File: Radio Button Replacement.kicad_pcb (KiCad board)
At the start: 2 copper layers, 40 x 40 mm, 19 parts, among them SW1 SW_Push_SPDT_1_3_2, SW2 SW_Push_SPDT_1_3_2, SW3 SW_Push_SPDT_1_3_2, SW4 SW_Push_SPDT_1_3_2

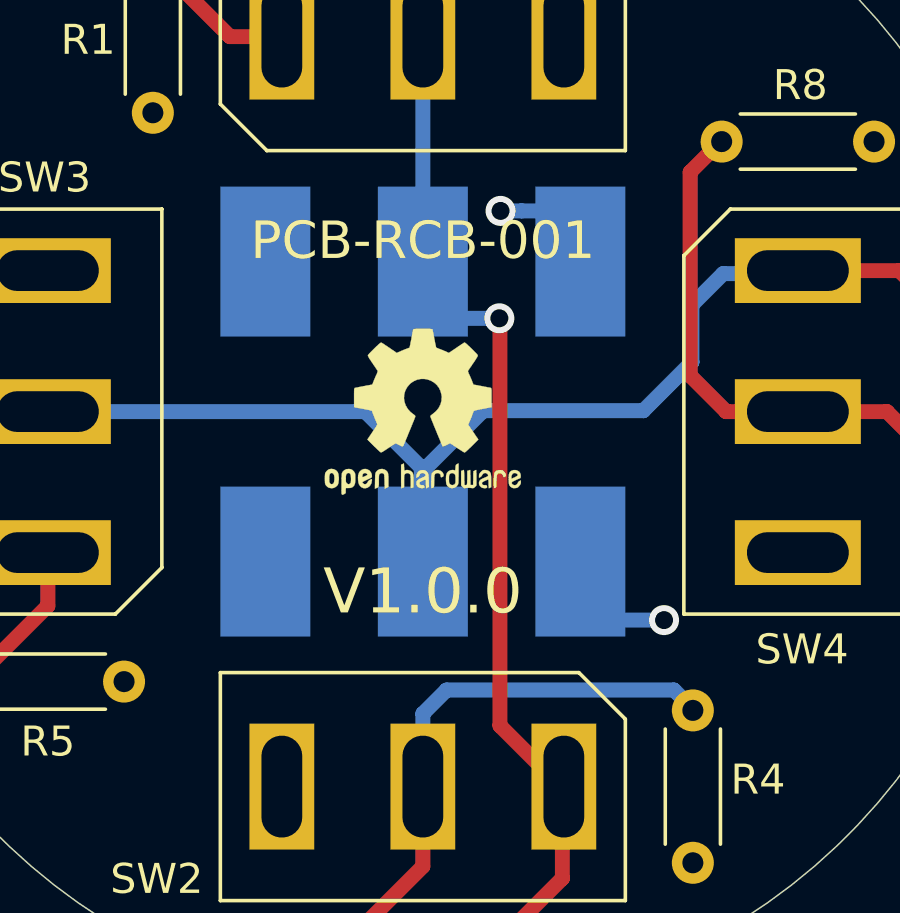
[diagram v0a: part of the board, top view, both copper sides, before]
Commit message: Update Radio Button Replacement.kicad_pcb
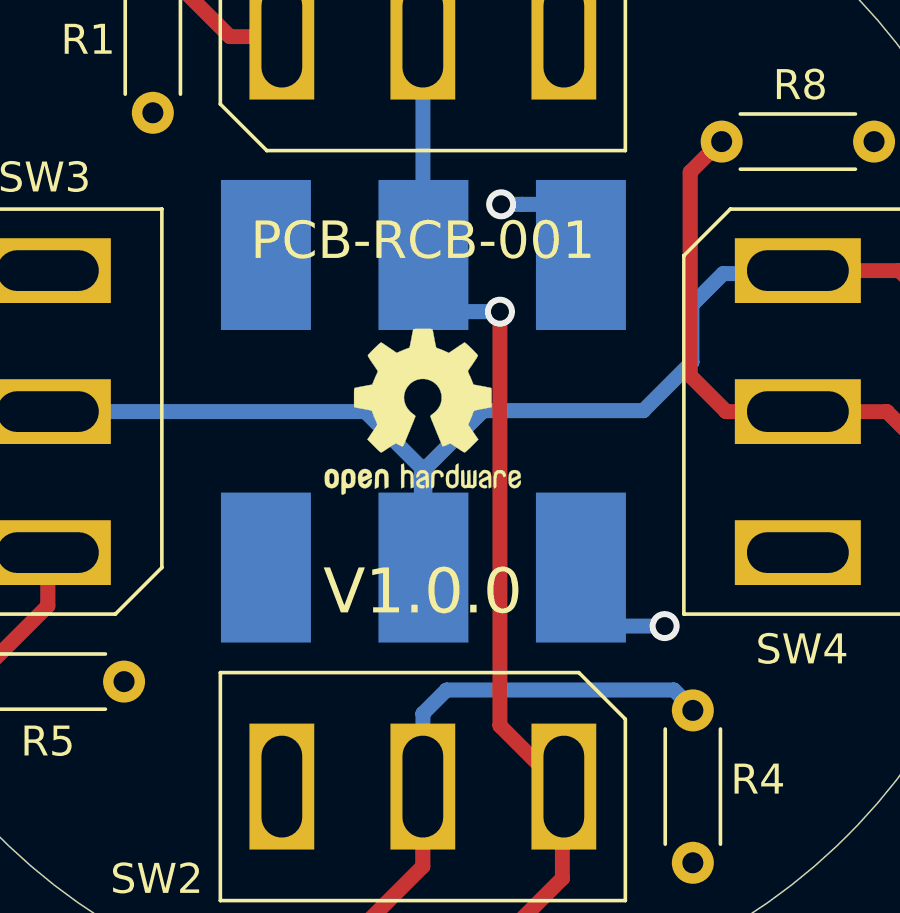
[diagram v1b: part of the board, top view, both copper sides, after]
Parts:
- moved TP1 0.22 mm to (150.0, 94.8)
- moved TP2 0.20 mm to (150.0, 105.2)
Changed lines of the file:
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@@
     (thickness 1.6)
     (drawings 5)
-    (tracks 68)
+    (tracks 67)
     (zones 0)
     (modules 19)
@@
     (31 B.Cu signal)
     (32 B.Adhes user)
-    (33 F.Adhes user hide)
+    (33 F.Adhes user)
     (34 B.Paste user)
     (35 F.Paste user)
     (36 B.SilkS user)
-    (37 F.SilkS user)
+    (37 F.SilkS user hide)
     (38 B.Mask user)
     (39 F.Mask user)
@@
   )
   (module Frequently_Used_LE:Pad_3_3.0-5.0 (layer B.Cu)
-    (at 150 105)
+    (at 150.02 105.2)
     (descr "SMD Pad 3.0x5.0 mm")
     (attr smd)
@@
       (effects (font (size 1 1) (thickness 0.15)) (justify top mirror))
     )
-    (fp_text user - (at -5.25 4.25) (layer B.SilkS)
+    (fp_text user - (at -5.22 -3.97) (layer B.SilkS)
       (effects (font (size 1.5 1.5) (thickness 0.3)) (justify mirror))
     )
-    (fp_text user S (at 0 4.25) (layer B.SilkS)
+    (fp_text user S (at 0.03 -3.97) (layer B.SilkS)
       (effects (font (size 1.5 1.5) (thickness 0.3)) (justify mirror))
     )
@@
     (fp_line (start 7.5 -3.25) (end -7.5 -3.25) (layer B.CrtYd) (width 0.05))
     (fp_line (start 7.5 3.25) (end 7.5 -3.25) (layer B.CrtYd) (width 0.05))
-    (fp_text user + (at 5.25 4.25) (layer B.SilkS)
+    (fp_text user + (at 5.28 -3.97) (layer B.SilkS)
       (effects (font (size 1.5 1.5) (thickness 0.3)) (justify mirror))
     )
@@
   )
   (module Frequently_Used_LE:Pad_3_3.0-5.0 (layer B.Cu)
-    (at 150 95)
+    (at 150.02 94.78)
     (descr "SMD Pad 3.0x5.0 mm")
     (attr smd)
@@
       (effects (font (size 1 1) (thickness 0.15)) (justify top mirror))
     )
-    (fp_text user - (at -5.25 4.25) (layer B.SilkS)
+    (fp_text user - (at -5.21 4.1) (layer B.SilkS)
       (effects (font (size 1.5 1.5) (thickness 0.3)) (justify mirror))
     )
-    (fp_text user S (at 0 4.25) (layer B.SilkS)
+    (fp_text user S (at 0.04 4.1) (layer B.SilkS)
       (effects (font (size 1.5 1.5) (thickness 0.3)) (justify mirror))
     )
@@
     (fp_line (start 7.5 -3.25) (end -7.5 -3.25) (layer B.CrtYd) (width 0.05))
     (fp_line (start 7.5 3.25) (end 7.5 -3.25) (layer B.CrtYd) (width 0.05))
-    (fp_text user + (at 5.25 4.25) (layer B.SilkS)
+    (fp_text user + (at 5.29 4.1) (layer B.SilkS)
       (effects (font (size 1.5 1.5) (thickness 0.3)) (justify mirror))
     )
@@
     (effects (font (size 1.25 1.25) (thickness 0.25)))
   )
-  (gr_text 2 (at 158.5 104.88) (layer B.SilkS)
+  (gr_text 2 (at 158.52 105.08) (layer B.SilkS)
     (effects (font (size 1.5 1.5) (thickness 0.3)) (justify mirror))
   )
-  (gr_text 1 (at 158.5 94.88) (layer B.SilkS)
+  (gr_text 1 (at 158.52 94.66) (layer B.SilkS)
     (effects (font (size 1.5 1.5) (thickness 0.3)) (justify mirror))
   )
@@
   (segment (start 150 95) (end 150 87.51) (width 0.5) (layer B.Cu) (net 3))
   (segment (start 145.44 112.6) (end 145.46 112.58) (width 0.5) (layer B.Cu) (net 0))
-  (via (at 158.04 106.95) (size 1) (drill 0.6) (layers F.Cu B.Cu) (net 1))
-  (segment (start 156.27 106.95) (end 158.04 106.95) (width 0.5) (layer B.Cu) (net 1))
+  (via (at 158.06 107.15) (size 1) (drill 0.6) (layers F.Cu B.Cu) (net 1))
+  (segment (start 156.29 107.15) (end 158.06 107.15) (width 0.5) (layer B.Cu) (net 1))
   (segment (start 155.25 105) (end 155.25 105.93) (width 0.5) (layer B.Cu) (net 1))
   (segment (start 155.25 105.93) (end 156.27 106.95) (width 0.5) (layer B.Cu) (net 1))
-  (via (at 152.59 93.31) (size 1) (drill 0.6) (layers F.Cu B.Cu) (net 1))
-  (segment (start 153.297106 93.31) (end 152.59 93.31) (width 0.5) (layer B.Cu) (net 1))
-  (segment (start 154.31 93.31) (end 153.297106 93.31) (width 0.5) (layer B.Cu) (net 1))
+  (via (at 152.61 93.09) (size 1) (drill 0.6) (layers F.Cu B.Cu) (net 1))
+  (segment (start 153.317106 93.09) (end 152.61 93.09) (width 0.5) (layer B.Cu) (net 1))
+  (segment (start 154.33 93.09) (end 153.317106 93.09) (width 0.5) (layer B.Cu) (net 1))
   (segment (start 155.25 95) (end 155.25 94.25) (width 0.5) (layer B.Cu) (net 1))
   (segment (start 155.25 94.25) (end 154.31 93.31) (width 0.5) (layer B.Cu) (net 1))
@@
   (segment (start 145.3 84.43) (end 147.41 82.32) (width 0.5) (layer F.Cu) (net 2))
   (segment (start 150.04 87.4) (end 150.19 87.55) (width 0.5) (layer B.Cu) (net 3))
-  (via (at 152.55 96.89) (size 1) (drill 0.6) (layers F.Cu B.Cu) (net 3))
-  (segment (start 150.55 96.89) (end 152.55 96.89) (width 0.5) (layer B.Cu) (net 3))
+  (via (at 152.57 96.67) (size 1) (drill 0.6) (layers F.Cu B.Cu) (net 3))
+  (segment (start 150.57 96.67) (end 152.57 96.67) (width 0.5) (layer B.Cu) (net 3))
   (segment (start 150 95) (end 150 96.34) (width 0.5) (layer B.Cu) (net 3))
   (segment (start 150 96.34) (end 150.55 96.89) (width 0.5) (layer B.Cu) (net 3))
-  (segment (start 152.57 96.91) (end 152.55 96.89) (width 0.5) (layer F.Cu) (net 3))
-  (segment (start 154.75 112.65) (end 152.57 110.47) (width 0.5) (layer F.Cu) (net 3))
-  (segment (start 152.57 110.47) (end 152.57 96.91) (width 0.5) (layer F.Cu) (net 3))
   (segment (start 154.65 115.56) (end 154.65 112.48) (width 0.5) (layer F.Cu) (net 3))
   (segment (start 152.55 117.66) (end 154.65 115.56) (width 0.5) (layer F.Cu) (net 3))
   (segment (start 150 87.5) (end 150 84.83) (width 0.5) (layer F.Cu) (net 3))
   (segment (start 150 84.83) (end 152.54 82.29) (width 0.5) (layer F.Cu) (net 3))
+  (segment (start 152.57 110.47) (end 152.57 96.67) (width 0.5) (layer F.Cu) (net 3))
+  (segment (start 154.75 112.65) (end 152.57 110.47) (width 0.5) (layer F.Cu) (net 3))
   (segment (start 158.98 109.84) (end 159 109.86) (width 0.5) (layer B.Cu) (net 4))
   (segment (start 150 110.07) (end 150.79 109.28) (width 0.5) (layer B.Cu) (net 4))

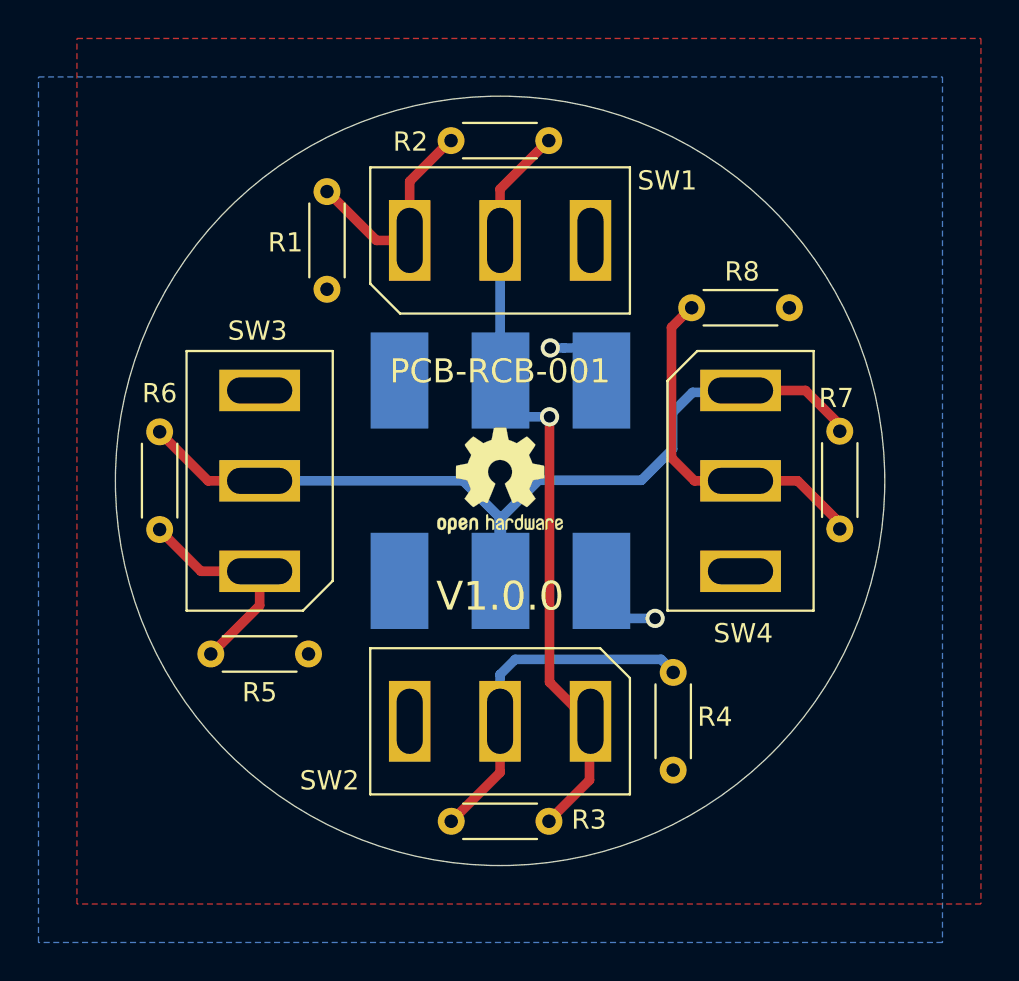
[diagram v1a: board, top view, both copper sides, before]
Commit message: Center marks added
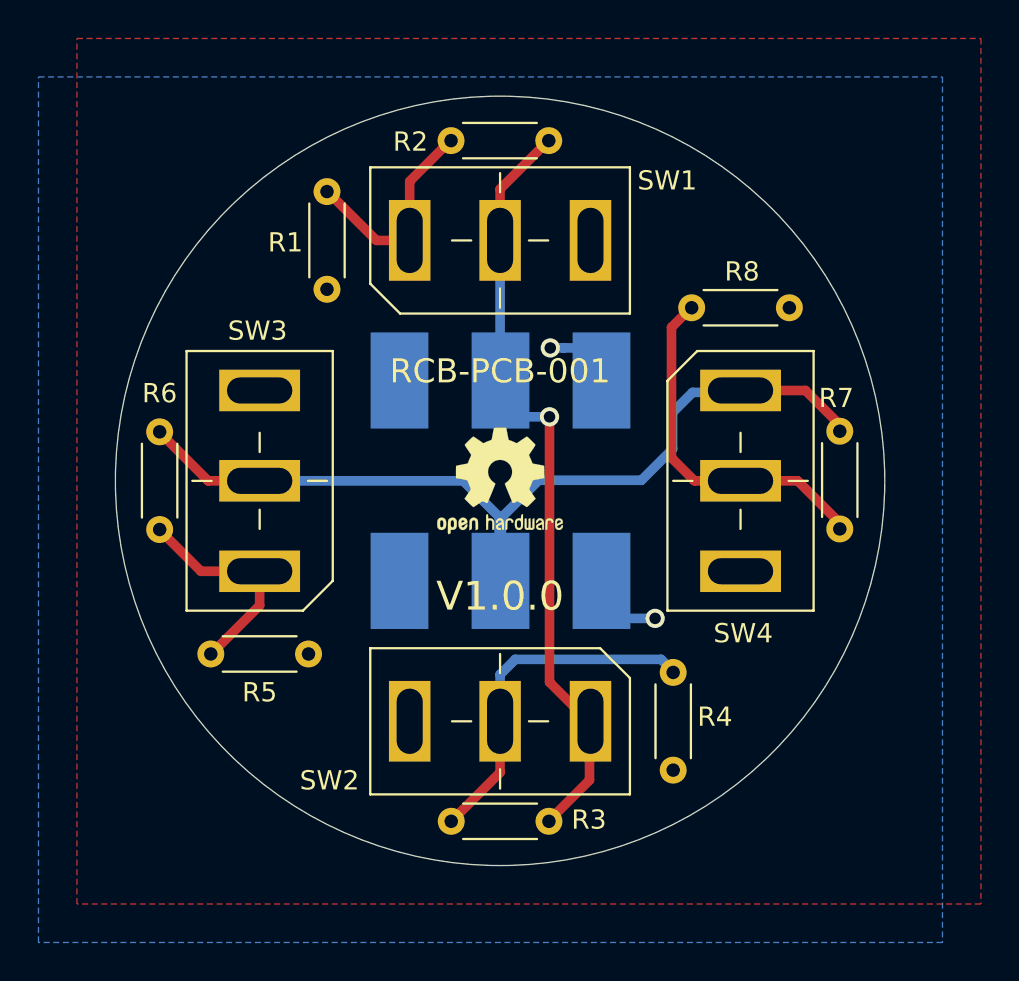
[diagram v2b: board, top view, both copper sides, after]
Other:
- board text added: "RCB-PCB-001"
- board text removed: "PCB-RCB-001"
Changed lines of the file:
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@@
     (35 F.Paste user)
     (36 B.SilkS user)
-    (37 F.SilkS user hide)
+    (37 F.SilkS user)
     (38 B.Mask user)
     (39 F.Mask user)
@@
     (aux_axis_origin 0 0)
     (grid_origin 150 100)
-    (visible_elements FFFFFF7F)
+    (visible_elements 7FFFFFFF)
     (pcbplotparams
       (layerselection 0x010fc_ffffffff)
@@
     (add_net "Net-(R5-Pad1)")
     (add_net "Net-(R7-Pad1)")
-    (add_net "Net-(SW1-Pad3)")
-    (add_net "Net-(SW3-Pad3)")
-    (add_net "Net-(SW4-Pad3)")
     (add_net VBUS)
-  )
-  (module Button_Switches_LE:ButtonCap (layer F.Cu)
-    (at 180.7 109.62)
-    (fp_text reference BC4 (at 0 -1.8) (layer F.Fab)
-      (effects (font (size 1 1) (thickness 0.15)))
-    )
-    (fp_text value "White 7.8 mm" (at 0 1.9) (layer F.Fab)
-      (effects (font (size 1 1) (thickness 0.15)))
-    )
-    (fp_arc (start 0 0) (end 0.6 0) (angle -180) (layer F.Fab) (width 0.12))
-    (fp_line (start 0.6 0.7) (end 0.6 0) (layer F.Fab) (width 0.12))
-    (fp_line (start -0.6 0.7) (end 0.6 0.7) (layer F.Fab) (width 0.12))
-    (fp_line (start -0.6 0) (end -0.6 0.7) (layer F.Fab) (width 0.12))
-  )
-  (module Button_Switches_LE:ButtonCap (layer F.Cu)
-    (at 180.7 103.06)
-    (fp_text reference BC3 (at 0 -1.8) (layer F.Fab)
-      (effects (font (size 1 1) (thickness 0.15)))
-    )
-    (fp_text value "Black 7.8 mm" (at 0 1.9) (layer F.Fab)
-      (effects (font (size 1 1) (thickness 0.15)))
-    )
-    (fp_arc (start 0 0) (end 0.6 0) (angle -180) (layer F.Fab) (width 0.12))
-    (fp_line (start 0.6 0.7) (end 0.6 0) (layer F.Fab) (width 0.12))
-    (fp_line (start -0.6 0.7) (end 0.6 0.7) (layer F.Fab) (width 0.12))
-    (fp_line (start -0.6 0) (end -0.6 0.7) (layer F.Fab) (width 0.12))
-  )
-  (module Button_Switches_LE:ButtonCap (layer F.Cu)
-    (at 180.7 96.45)
-    (fp_text reference BC2 (at 0 -1.8) (layer F.Fab)
-      (effects (font (size 1 1) (thickness 0.15)))
-    )
-    (fp_text value "Black 7.8 mm" (at 0 1.9) (layer F.Fab)
-      (effects (font (size 1 1) (thickness 0.15)))
-    )
-    (fp_arc (start 0 0) (end 0.6 0) (angle -180) (layer F.Fab) (width 0.12))
-    (fp_line (start 0.6 0.7) (end 0.6 0) (layer F.Fab) (width 0.12))
-    (fp_line (start -0.6 0.7) (end 0.6 0.7) (layer F.Fab) (width 0.12))
-    (fp_line (start -0.6 0) (end -0.6 0.7) (layer F.Fab) (width 0.12))
-  )
-  (module Button_Switches_LE:ButtonCap (layer F.Cu)
-    (at 180.7 89.57)
-    (fp_text reference BC1 (at 0 -1.8) (layer F.Fab)
-      (effects (font (size 1 1) (thickness 0.15)))
-    )
-    (fp_text value "Red 7.8 mm" (at 0 1.9) (layer F.Fab)
-      (effects (font (size 1 1) (thickness 0.15)))
-    )
-    (fp_arc (start 0 0) (end 0.6 0) (angle -180) (layer F.Fab) (width 0.12))
-    (fp_line (start 0.6 0.7) (end 0.6 0) (layer F.Fab) (width 0.12))
-    (fp_line (start -0.6 0.7) (end 0.6 0.7) (layer F.Fab) (width 0.12))
-    (fp_line (start -0.6 0) (end -0.6 0.7) (layer F.Fab) (width 0.12))
   )
   (module Button_Switches_LE:8125SHZ (layer F.Cu)
@@
       (effects (font (size 1 1) (thickness 0.15)))
     )
+    (fp_line (start -2.5 0) (end -3.5 0) (layer F.SilkS) (width 0.12))
+    (fp_line (start 3.5 0) (end 2.5 0) (layer F.SilkS) (width 0.12))
+    (fp_line (start 0 2.5) (end 0 1.5) (layer F.SilkS) (width 0.12))
+    (fp_line (start 0 -1.5) (end 0 -2.5) (layer F.SilkS) (width 0.12))
     (fp_text user NC (at 3.179524 6.1525 unlocked) (layer B.SilkS)
       (effects (font (size 1.25 1.25) (thickness 0.2)) (justify left mirror))
@@
       (effects (font (size 1 1) (thickness 0.15)))
     )
+    (fp_line (start -2.5 0) (end -3.5 0) (layer F.SilkS) (width 0.12))
+    (fp_line (start 3.5 0) (end 2.5 0) (layer F.SilkS) (width 0.12))
+    (fp_line (start 0 2.5) (end 0 1.5) (layer F.SilkS) (width 0.12))
+    (fp_line (start 0 -1.5) (end 0 -2.5) (layer F.SilkS) (width 0.12))
     (fp_text user NC (at 3.299524 3.2825 unlocked) (layer B.SilkS)
       (effects (font (size 1.25 1.25) (thickness 0.2)) (justify left mirror))
@@
       (effects (font (size 1 1) (thickness 0.15)))
     )
+    (fp_line (start -2.5 0) (end -3.5 0) (layer F.SilkS) (width 0.12))
+    (fp_line (start 3.5 0) (end 2.5 0) (layer F.SilkS) (width 0.12))
+    (fp_line (start 0 2.5) (end 0 1.5) (layer F.SilkS) (width 0.12))
+    (fp_line (start 0 -1.5) (end 0 -2.5) (layer F.SilkS) (width 0.12))
     (fp_text user NC (at 2.369524 4.6525 unlocked) (layer B.SilkS)
       (effects (font (size 1.25 1.25) (thickness 0.2)) (justify left mirror))
@@
       (effects (font (size 1 1) (thickness 0.15)))
     )
+    (fp_line (start -2.5 0) (end -3.5 0) (layer F.SilkS) (width 0.12))
+    (fp_line (start 3.5 0) (end 2.5 0) (layer F.SilkS) (width 0.12))
+    (fp_line (start 0 2.5) (end 0 1.5) (layer F.SilkS) (width 0.12))
+    (fp_line (start 0 -1.5) (end 0 -2.5) (layer F.SilkS) (width 0.12))
     (fp_text user NC (at 5.249524 4.6825 unlocked) (layer B.SilkS)
       (effects (font (size 1.25 1.25) (thickness 0.2)) (justify left mirror))
@@
       (rotate (xyz -90 0 90))
     )
+  )
+  (module Button_Switches_LE:ButtonCap (layer F.Cu)
+    (at 180.7 109.62)
+    (fp_text reference BC4 (at 0 -1.8) (layer F.Fab)
+      (effects (font (size 1 1) (thickness 0.15)))
+    )
+    (fp_text value "White 7.8 mm" (at 0 1.9) (layer F.Fab)
+      (effects (font (size 1 1) (thickness 0.15)))
+    )
+    (fp_arc (start 0 0) (end 0.6 0) (angle -180) (layer F.Fab) (width 0.12))
+    (fp_line (start 0.6 0.7) (end 0.6 0) (layer F.Fab) (width 0.12))
+    (fp_line (start -0.6 0.7) (end 0.6 0.7) (layer F.Fab) (width 0.12))
+    (fp_line (start -0.6 0) (end -0.6 0.7) (layer F.Fab) (width 0.12))
+  )
+  (module Button_Switches_LE:ButtonCap (layer F.Cu)
+    (at 180.7 103.06)
+    (fp_text reference BC3 (at 0 -1.8) (layer F.Fab)
+      (effects (font (size 1 1) (thickness 0.15)))
+    )
+    (fp_text value "Black 7.8 mm" (at 0 1.9) (layer F.Fab)
+      (effects (font (size 1 1) (thickness 0.15)))
+    )
+    (fp_arc (start 0 0) (end 0.6 0) (angle -180) (layer F.Fab) (width 0.12))
+    (fp_line (start 0.6 0.7) (end 0.6 0) (layer F.Fab) (width 0.12))
+    (fp_line (start -0.6 0.7) (end 0.6 0.7) (layer F.Fab) (width 0.12))
+    (fp_line (start -0.6 0) (end -0.6 0.7) (layer F.Fab) (width 0.12))
+  )
+  (module Button_Switches_LE:ButtonCap (layer F.Cu)
+    (at 180.7 96.45)
+    (fp_text reference BC2 (at 0 -1.8) (layer F.Fab)
+      (effects (font (size 1 1) (thickness 0.15)))
+    )
+    (fp_text value "Black 7.8 mm" (at 0 1.9) (layer F.Fab)
+      (effects (font (size 1 1) (thickness 0.15)))
+    )
+    (fp_arc (start 0 0) (end 0.6 0) (angle -180) (layer F.Fab) (width 0.12))
+    (fp_line (start 0.6 0.7) (end 0.6 0) (layer F.Fab) (width 0.12))
+    (fp_line (start -0.6 0.7) (end 0.6 0.7) (layer F.Fab) (width 0.12))
+    (fp_line (start -0.6 0) (end -0.6 0.7) (layer F.Fab) (width 0.12))
+  )
+  (module Button_Switches_LE:ButtonCap (layer F.Cu)
+    (at 180.7 89.57)
+    (fp_text reference BC1 (at 0 -1.8) (layer F.Fab)
+      (effects (font (size 1 1) (thickness 0.15)))
+    )
+    (fp_text value "Red 7.8 mm" (at 0 1.9) (layer F.Fab)
+      (effects (font (size 1 1) (thickness 0.15)))
+    )
+    (fp_arc (start 0 0) (end 0.6 0) (angle -180) (layer F.Fab) (width 0.12))
+    (fp_line (start 0.6 0.7) (end 0.6 0) (layer F.Fab) (width 0.12))
+    (fp_line (start -0.6 0.7) (end 0.6 0.7) (layer F.Fab) (width 0.12))
+    (fp_line (start -0.6 0) (end -0.6 0.7) (layer F.Fab) (width 0.12))
   )
   (module Logos:OSHW-Logo2_7.3x6mm_SilkScreen (layer F.Cu)
@@
     (effects (font (size 1.5 1.5) (thickness 0.3)))
   )
-  (gr_text PCB-RCB-001 (at 150 94.3) (layer F.SilkS)
+  (gr_text RCB-PCB-001 (at 150 94.3) (layer F.SilkS)
     (effects (font (size 1.25 1.25) (thickness 0.25)))
   )
@@
   )
   (gr_circle (center 150 100) (end 170 100) (layer Edge.Cuts) (width 0.05))
-  (segment (start 150 87.51) (end 150.06 87.45) (width 0.5) (layer B.Cu) (net 3))
-  (segment (start 150 95) (end 150 87.51) (width 0.5) (layer B.Cu) (net 3))
   (segment (start 145.44 112.6) (end 145.46 112.58) (width 0.5) (layer B.Cu) (net 0))
   (via (at 158.06 107.15) (size 1) (drill 0.6) (layers F.Cu B.Cu) (net 1))
@@
   (segment (start 145.3 87.5) (end 145.3 84.43) (width 0.5) (layer F.Cu) (net 2))
   (segment (start 145.3 84.43) (end 147.41 82.32) (width 0.5) (layer F.Cu) (net 2))
+  (segment (start 150 87.51) (end 150.06 87.45) (width 0.5) (layer B.Cu) (net 3))
+  (segment (start 150 95) (end 150 87.51) (width 0.5) (layer B.Cu) (net 3))
   (segment (start 150.04 87.4) (end 150.19 87.55) (width 0.5) (layer B.Cu) (net 3))
   (via (at 152.57 96.67) (size 1) (drill 0.6) (layers F.Cu B.Cu) (net 3))
